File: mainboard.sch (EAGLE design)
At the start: 46 parts, among them IC1 DS1307, IC2 LM2596S, J1 AVR_SPI_PRG_6PTH, Q1 32.768 kHz, U1 ATMEGA328P, U2 3.3V, U3 5V, U4 MMA7660FCR1

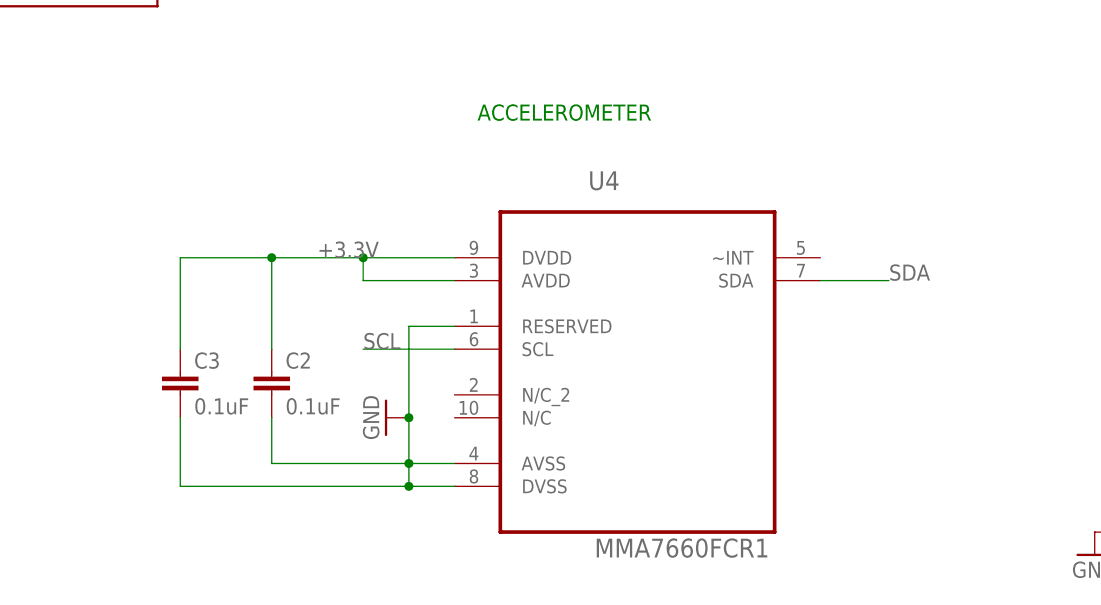
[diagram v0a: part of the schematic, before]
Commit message: added lbr for MMA8653. changed accelerometer to MMA8653.
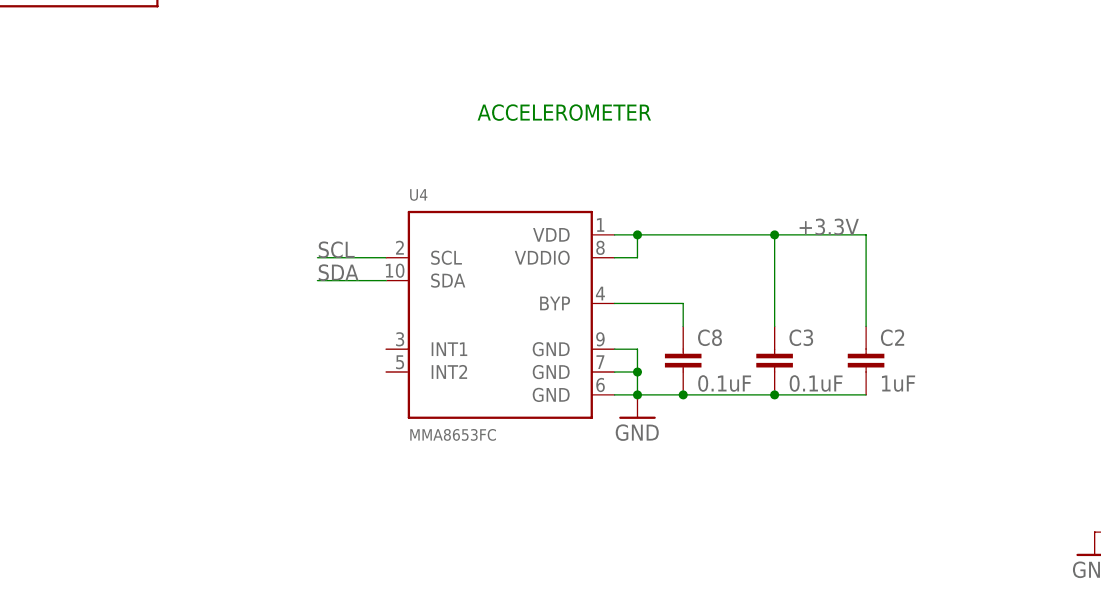
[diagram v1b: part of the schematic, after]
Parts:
- added C8: 0.1uF, SparkFun-Capacitors:CAP0603-CAP
- C2: value 0.1uF -> 1uF
- U4: value MMA7660FCR1 -> MMA8653FC; device Freescale_By_element14_Batch_1:MMA7660FCR1 -> logic-supply:MMA8653FC
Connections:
- new net N$16: C8.1, U4.BYP
- net +3.3V: now also U4.VDD, U4.VDDIO; no longer U4.AVDD, U4.DVDD
- net GND: now also C8.2, U4.GND@1, U4.GND@2, U4.GND@3; no longer U4.AVSS, U4.DVSS, U4.RESERVED
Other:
- moved on the sheet: C2, C3
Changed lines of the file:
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@@
 <?xml version="1.0" encoding="utf-8"?>
 <!DOCTYPE eagle SYSTEM "eagle.dtd">
-<eagle version="6.5.0">
+<eagle version="6.3">
 <drawing>
 <settings>
@@
 <part name="GND15" library="supply1" deviceset="GND" device=""/>
 <part name="GND16" library="supply1" deviceset="GND" device=""/>
-<part name="U4" library="Freescale_By_element14_Batch_1" deviceset="MMA7660FCR1" device=""/>
-<part name="GND17" library="supply1" deviceset="GND" device=""/>
-<part name="C2" library="SparkFun-Capacitors" deviceset="CAP" device="0603-CAP" value="0.1uF"/>
-<part name="C3" library="SparkFun-Capacitors" deviceset="CAP" device="0603-CAP" value="0.1uF"/>
 <part name="R10" library="SparkFun-Resistors" deviceset="RESISTOR" device="0603-RES" value="1.8K"/>
 <part name="C4" library="SparkFun-Capacitors" deviceset="CAP" device="0603-CAP" value="0.1uF"/>
@@
 <part name="GND29" library="supply1" deviceset="GND" device=""/>
 <part name="R17" library="SparkFun-Resistors" deviceset="RESISTOR" device="0603" value="10k"/>
+<part name="U4" library="logic-supply" deviceset="MMA8653" device="FC"/>
+<part name="C3" library="SparkFun-Capacitors" deviceset="CAP" device="0603-CAP" value="0.1uF"/>
+<part name="C2" library="SparkFun-Capacitors" deviceset="CAP" device="0603-CAP" value="1uF"/>
+<part name="C8" library="SparkFun-Capacitors" deviceset="CAP" device="0603-CAP" value="0.1uF"/>
+<part name="GND30" library="supply1" deviceset="GND" device=""/>
 </parts>
 <sheets>
@@
 <instance part="GND15" gate="1" x="58.42" y="-43.18"/>
 <instance part="GND16" gate="1" x="96.52" y="91.44" rot="R270"/>
-<instance part="U4" gate="A" x="162.56" y="-40.64"/>
-<instance part="GND17" gate="1" x="134.62" y="-48.26" rot="R270"/>
-<instance part="C2" gate="G$1" x="121.92" y="-45.72"/>
-<instance part="C3" gate="G$1" x="111.76" y="-45.72"/>
 <instance part="R10" gate="G$1" x="167.64" y="93.98" rot="R90"/>
 <instance part="C4" gate="G$1" x="124.46" y="91.44"/>
@@
 <instance part="GND29" gate="1" x="12.7" y="88.9"/>
 <instance part="R17" gate="G$1" x="5.08" y="99.06" rot="R90"/>
+<instance part="U4" gate="G$1" x="147.32" y="-35.56"/>
+<instance part="C3" gate="G$1" x="177.8" y="-43.18"/>
+<instance part="C2" gate="G$1" x="187.96" y="-43.18"/>
+<instance part="C8" gate="G$1" x="167.64" y="-43.18"/>
+<instance part="GND30" gate="1" x="162.56" y="-48.26"/>
 </instances>
 <busses>
@@
 </segment>
 <segment>
-<pinref part="U4" gate="A" pin="SDA"/>
-<wire x1="182.88" y1="-33.02" x2="190.5" y2="-33.02" width="0.1524" layer="91"/>
-<label x="190.5" y="-33.02" size="1.778" layer="95"/>
-</segment>
-<segment>
 <pinref part="IC1" gate="G$1" pin="SDA"/>
 <wire x1="254" y1="-45.72" x2="266.7" y2="-45.72" width="0.1524" layer="91"/>
 <label x="266.7" y="-45.72" size="1.778" layer="95"/>
 </segment>
+<segment>
+<pinref part="U4" gate="G$1" pin="SDA"/>
+<wire x1="134.62" y1="-33.02" x2="127" y2="-33.02" width="0.1524" layer="91"/>
+<label x="127" y="-33.02" size="1.778" layer="95"/>
+</segment>
 </net>
 <net name="SCL" class="0">
@@
 </segment>
 <segment>
-<pinref part="U4" gate="A" pin="SCL"/>
-<wire x1="142.24" y1="-40.64" x2="132.08" y2="-40.64" width="0.1524" layer="91"/>
-<label x="132.08" y="-40.64" size="1.778" layer="95"/>
-</segment>
-<segment>
 <pinref part="IC1" gate="G$1" pin="SCL"/>
 <wire x1="254" y1="-40.64" x2="266.7" y2="-40.64" width="0.1524" layer="91"/>
 <label x="266.7" y="-40.64" size="1.778" layer="95"/>
+</segment>
+<segment>
+<pinref part="U4" gate="G$1" pin="SCL"/>
+<wire x1="134.62" y1="-30.48" x2="127" y2="-30.48" width="0.1524" layer="91"/>
+<label x="127" y="-30.48" size="1.778" layer="95"/>
 </segment>
 </net>
@@
 </segment>
 <segment>
-<pinref part="U4" gate="A" pin="DVDD"/>
-<wire x1="142.24" y1="-30.48" x2="132.08" y2="-30.48" width="0.1524" layer="91"/>
-<pinref part="C3" gate="G$1" pin="1"/>
-<wire x1="132.08" y1="-30.48" x2="121.92" y2="-30.48" width="0.1524" layer="91"/>
-<wire x1="121.92" y1="-30.48" x2="111.76" y2="-30.48" width="0.1524" layer="91"/>
-<wire x1="111.76" y1="-30.48" x2="111.76" y2="-40.64" width="0.1524" layer="91"/>
-<pinref part="C2" gate="G$1" pin="1"/>
-<wire x1="121.92" y1="-40.64" x2="121.92" y2="-30.48" width="0.1524" layer="91"/>
-<pinref part="U4" gate="A" pin="AVDD"/>
-<wire x1="142.24" y1="-33.02" x2="132.08" y2="-33.02" width="0.1524" layer="91"/>
-<wire x1="132.08" y1="-33.02" x2="132.08" y2="-30.48" width="0.1524" layer="91"/>
-<label x="127" y="-30.48" size="1.778" layer="95"/>
-<junction x="132.08" y="-30.48"/>
-<junction x="121.92" y="-30.48"/>
-</segment>
-<segment>
 <pinref part="R10" gate="G$1" pin="2"/>
 <wire x1="154.94" y1="99.06" x2="167.64" y2="99.06" width="0.1524" layer="91"/>
@@
 <wire x1="182.88" y1="99.06" x2="198.12" y2="99.06" width="0.1524" layer="91"/>
 <label x="182.88" y="99.06" size="1.778" layer="95"/>
+</segment>
+<segment>
+<pinref part="U4" gate="G$1" pin="VDD"/>
+<wire x1="160.02" y1="-27.94" x2="162.56" y2="-27.94" width="0.1524" layer="91"/>
+<wire x1="162.56" y1="-27.94" x2="177.8" y2="-27.94" width="0.1524" layer="91"/>
+<wire x1="177.8" y1="-27.94" x2="187.96" y2="-27.94" width="0.1524" layer="91"/>
+<pinref part="C3" gate="G$1" pin="1"/>
+<wire x1="177.8" y1="-27.94" x2="177.8" y2="-38.1" width="0.1524" layer="91"/>
+<pinref part="U4" gate="G$1" pin="VDDIO"/>
+<wire x1="160.02" y1="-30.48" x2="162.56" y2="-30.48" width="0.1524" layer="91"/>
+<wire x1="162.56" y1="-30.48" x2="162.56" y2="-27.94" width="0.1524" layer="91"/>
+<junction x="162.56" y="-27.94"/>
+<junction x="177.8" y="-27.94"/>
+<label x="180.34" y="-27.94" size="1.778" layer="95"/>
+<pinref part="C2" gate="G$1" pin="1"/>
+<wire x1="187.96" y1="-27.94" x2="187.96" y2="-38.1" width="0.1524" layer="91"/>
 </segment>
 </net>
@@
 </segment>
 <segment>
-<pinref part="U4" gate="A" pin="RESERVED"/>
-<wire x1="142.24" y1="-38.1" x2="137.16" y2="-38.1" width="0.1524" layer="91"/>
-<wire x1="137.16" y1="-38.1" x2="137.16" y2="-48.26" width="0.1524" layer="91"/>
-<pinref part="U4" gate="A" pin="DVSS"/>
-<wire x1="137.16" y1="-48.26" x2="137.16" y2="-53.34" width="0.1524" layer="91"/>
-<wire x1="137.16" y1="-53.34" x2="137.16" y2="-55.88" width="0.1524" layer="91"/>
-<wire x1="137.16" y1="-55.88" x2="142.24" y2="-55.88" width="0.1524" layer="91"/>
-<pinref part="U4" gate="A" pin="AVSS"/>
-<wire x1="142.24" y1="-53.34" x2="137.16" y2="-53.34" width="0.1524" layer="91"/>
-<pinref part="GND17" gate="1" pin="GND"/>
-<junction x="137.16" y="-48.26"/>
-<pinref part="C2" gate="G$1" pin="2"/>
-<wire x1="121.92" y1="-53.34" x2="137.16" y2="-53.34" width="0.1524" layer="91"/>
-<wire x1="121.92" y1="-48.26" x2="121.92" y2="-53.34" width="0.1524" layer="91"/>
-<wire x1="137.16" y1="-55.88" x2="111.76" y2="-55.88" width="0.1524" layer="91"/>
-<pinref part="C3" gate="G$1" pin="2"/>
-<wire x1="111.76" y1="-55.88" x2="111.76" y2="-48.26" width="0.1524" layer="91"/>
-<junction x="137.16" y="-55.88"/>
-<junction x="137.16" y="-53.34"/>
-</segment>
-<segment>
 <pinref part="C4" gate="G$1" pin="2"/>
 <pinref part="GND18" gate="1" pin="GND"/>
@@
 <pinref part="GND28" gate="1" pin="GND"/>
 </segment>
-</net>
+<segment>
+<pinref part="U4" gate="G$1" pin="GND@3"/>
+<wire x1="160.02" y1="-40.64" x2="162.56" y2="-40.64" width="0.1524" layer="91"/>
+<wire x1="162.56" y1="-40.64" x2="162.56" y2="-43.18" width="0.1524" layer="91"/>
+<pinref part="U4" gate="G$1" pin="GND@2"/>
+<wire x1="160.02" y1="-43.18" x2="162.56" y2="-43.18" width="0.1524" layer="91"/>
+<wire x1="162.56" y1="-43.18" x2="162.56" y2="-45.72" width="0.1524" layer="91"/>
+<pinref part="U4" gate="G$1" pin="GND@1"/>
+<wire x1="162.56" y1="-45.72" x2="160.02" y2="-45.72" width="0.1524" layer="91"/>
+<wire x1="162.56" y1="-45.72" x2="167.64" y2="-45.72" width="0.1524" layer="91"/>
+<wire x1="167.64" y1="-45.72" x2="177.8" y2="-45.72" width="0.1524" layer="91"/>
+<pinref part="C3" gate="G$1" pin="2"/>
+<pinref part="C8" gate="G$1" pin="2"/>
+<junction x="162.56" y="-43.18"/>
+<junction x="162.56" y="-45.72"/>
+<junction x="167.64" y="-45.72"/>
+<pinref part="GND30" gate="1" pin="GND"/>
+<pinref part="C2" gate="G$1" pin="2"/>
+<wire x1="187.96" y1="-45.72" x2="177.8" y2="-45.72" width="0.1524" layer="91"/>
+<junction x="177.8" y="-45.72"/>
+</segment>
+</net>
+<net name="N$16" class="0">
+<segment>
+<pinref part="U4" gate="G$1" pin="BYP"/>
+<wire x1="160.02" y1="-35.56" x2="167.64" y2="-35.56" width="0.1524" layer="91"/>
+<pinref part="C8" gate="G$1" pin="1"/>
+<wire x1="167.64" y1="-35.56" x2="167.64" y2="-38.1" width="0.1524" layer="91"/>
+</segment>
+</net>
